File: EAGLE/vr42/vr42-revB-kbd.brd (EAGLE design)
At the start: 226.6 x 74.2 mm, 176 parts, among them M0 74HC589A_DT, M1 74HC589A_DT, M2 74HC589A_DT, M3 74HC589A_DT, M4 74HC589A_DT, M5 74HC589A_DT, U1 2N7002

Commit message: Rev 1.0B
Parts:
- removed C10, C11, C12, C13, C14, C15, C16, C17, C18, C19, C20, C21, C22, C23, C24, C25, C26, C27, C28, C7, C8, C9: 1uF, rcl:C0603
- added CA1, CA11, CA13, CA15, CA17, CA19, CA21, CA23, CA25, CA27, CA29, CA3, CA31, CA33, CA35, CA37, CA39, CA41, CA43, CA5, CA6, CA7, CA9: 1uF, rcl:C0603
- added LOGO1: OSHW-LOGOL, random_logos:OSHW-LOGO-L
- added U$3: TECSMITH-LOGOLONG, random_logos:TECSMITH-NAME
- added U$4: QMK_LOGO, random_logos:QMK_LOGO
- moved R45 12.4 mm to (210.8, 37.4), turned to 270 degrees
- moved R20 7.04 mm to (189.7, 68.5), turned to 180 degrees
- moved R36 7.00 mm to (108.7, 30.4), turned to 180 degrees
- moved R4 6.94 mm to (37.3, 68.5), turned to 180 degrees
- moved R11 6.90 mm to (94.4, 68.5), turned to 180 degrees
- moved R29 3.67 mm to (54.1, 24.9), turned to 270 degrees
- moved R27 3.39 mm to (32.6, 30.4), turned to 180 degrees
- moved R7 2.10 mm to (25.6, 45.0)
- moved C2 1.50 mm to (90.5, 57.0)
- moved C3 0.85 mm to (186.0, 57.6)
- moved R49 0.76 mm to (208.8, 37.4)
- moved C6 0.50 mm to (205.3, 20.1)
- renumbered I1 to A1, I10 to A10, I11 to A11, I12 to A12, I13 to A13, I14 to A14, I15 to A15, I16 to A16, I17 to A17, I18 to A18, I19 to A19, I2 to A2, I20 to A20, I21 to A21, I22 to A22, I23 to A23, I24 to A24, I25 to A25, I26 to A26, I27 to A27, I28 to A28, I29 to A29, I3 to A3, I30 to A30, I31 to A31, I32 to A32, I33 to A33, I34 to A34, I35 to A35, I36 to A36, I37 to A37, I38 to A38, I39 to A39, I4 to A4, I40 to A40, I41 to A41, I42 to A42, I43 to A43, I5 to A5, I6 to A6, I7 to A7, I8 to A8, I9 to A9
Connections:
- net GND: now also CA1.2, CA11.2, CA13.2, CA15.2, CA17.2, CA19.2, CA21.2, CA23.2, CA25.2, CA27.2, CA29.2, CA3.2, CA31.2, CA33.2, CA35.2, CA37.2, CA39.2, CA41.2, CA43.2, CA5.2, CA6.2, CA7.2, CA9.2; no longer C10.2, C11.2, C12.2, C13.2, C14.2, C15.2, C16.2, C17.2, C18.2, C19.2, C20.2, C21.2, C22.2, C23.2, C24.2, C25.2, C26.2, C27.2, C28.2, C7.2, C8.2, C9.2
- net VCC_1: now also CA1.1, CA11.1, CA13.1, CA15.1, CA17.1, CA19.1, CA21.1, CA23.1, CA25.1, CA27.1, CA29.1, CA3.1, CA31.1, CA33.1, CA35.1, CA37.1, CA39.1, CA41.1, CA43.1, CA5.1, CA6.1, CA7.1, CA9.1; no longer C10.1, C11.1, C12.1, C13.1, C14.1, C15.1, C16.1, C17.1, C18.1, C19.1, C20.1, C21.1, C22.1, C23.1, C24.1, C25.1, C26.1, C27.1, C28.1, C7.1, C8.1, C9.1
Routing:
- net VCC_1: track 0.00 -> 1149.0 mm, vias 0 -> 50
- net LATCH_MTX: track 266.4 -> 430.3 mm, vias 6 -> 7
- net SCK: track 252.8 -> 416.2 mm, vias 5 -> 8
- net CS_MTX: track 256.6 -> 418.0 mm, vias 3 -> 6
- net MATRIX_1_2: track 0.00 -> 109.9 mm, vias 0 -> 4
- net K50: track 5.67 -> 99.2 mm, vias 0 -> 6
- net VCC_2: track 1159.9 -> 1232.3 mm, vias 3 -> 12
- net MATRIX_0_1: track 0.00 -> 65.0 mm, vias 0 -> 2
- net K54: track 5.67 -> 70.0 mm, vias 0 -> 2
- net K44: track 5.67 -> 67.5 mm, vias 0 -> 2
- net K13: track 5.67 -> 66.4 mm, vias 0 -> 2
- net K17: track 5.67 -> 59.3 mm
- net K51: track 5.67 -> 59.2 mm, vias 0 -> 4
- net K40: track 5.67 -> 55.6 mm
- net K32: track 5.67 -> 48.9 mm
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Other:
- board text added: "(c) 2024 Vino Rodrigues https://c1k.it/vr42"
- board text added: "Revision: 1.0B"
- board text added: "VR42 Keyboard Key PCB"

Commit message: .
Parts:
- added U$5, U$6, U$7: FIDUCIAL, __temp_to_delete:FIDUCIAL
- moved I44 0.20 mm to (224.5, 51.3)
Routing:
- net VCC_1: track 1149.0 -> 1142.3 mm
- net VCC_2: track 1232.3 -> 1228.9 mm
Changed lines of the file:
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@@
 <element name="SW_Y" library="ts_keyboards" package="MX-5-PIN-HOTSWAP-PAD" value="MX-5-PIN-HOTSWAP-PAD" x="123.825" y="66.675" smashed="yes"/>
 <element name="SW_Z" library="ts_keyboards" package="MX-5-PIN-HOTSWAP-PAD" value="MX-5-PIN-HOTSWAP-PAD" x="42.8625" y="28.575" smashed="yes"/>
-<element name="I44" library="__temp_to_delete" package="ARGB" value="ARGB" x="224.3" y="51.3" smashed="yes" rot="R270"/>
+<element name="I44" library="__temp_to_delete" package="ARGB" value="ARGB" x="224.5" y="51.3" smashed="yes" rot="R270"/>
 <element name="M5" library="__untitled" package="TSSOP16" value="74HC589A_DT" x="209.5" y="23.5" smashed="yes" rot="MR270">
 <attribute name="NAME" x="209.9" y="24.4" size="1.016" layer="28" ratio="6" rot="SMR270"/>
@@
 <element name="U$4" library="random_logos" package="QMK_LOGO" value="QMK_LOGO" x="64" y="37" smashed="yes" rot="MR0"/>
 <element name="LOGO1" library="random_logos" package="OSHW-LOGO-L" value="OSHW-LOGOL" x="189" y="36" smashed="yes" rot="MR0"/>
+<element name="U$5" library="__temp_to_delete" package="FIDUCIAL" value="FIDUCIAL" x="3.5" y="72.5" smashed="yes"/>
+<element name="U$6" library="__temp_to_delete" package="FIDUCIAL" value="FIDUCIAL" x="224.5" y="20.5" smashed="yes"/>
+<element name="U$7" library="__temp_to_delete" package="FIDUCIAL" value="FIDUCIAL" x="72" y="3.5" smashed="yes"/>
 </elements>
 <signals>
@@
 <wire x1="205" y1="33.655" x2="221.615" y2="33.655" width="0.4064" layer="1"/>
 <wire x1="226.357" y1="70.1" x2="226.357" y2="52.705" width="0.4064" layer="1"/>
-<wire x1="226.357" y1="52.705" x2="226.357" y2="40.35" width="0.4064" layer="1"/>
 <wire x1="140.6525" y1="33.655" x2="121.6025" y2="33.655" width="0.4064" layer="1"/>
 <wire x1="121.6025" y1="33.655" x2="102.5525" y2="33.655" width="0.4064" layer="1"/>
@@
 <wire x1="40.65" y1="54.905" x2="38.0775" y2="54.905" width="0.4064" layer="1"/>
 <wire x1="38.0775" y1="54.905" x2="35.8775" y2="52.705" width="0.4064" layer="1"/>
-<wire x1="12.065" y1="71.755" x2="3.755" y2="71.755" width="0.4064" layer="1"/>
-<wire x1="3.755" y1="71.755" x2="2.243" y2="70.243" width="0.4064" layer="1"/>
-<wire x1="2.243" y1="70.243" x2="2.243" y2="56" width="0.4064" layer="1"/>
-<wire x1="2.243" y1="56" x2="2.243" y2="52.705" width="0.4064" layer="1"/>
 <wire x1="2.238" y1="52.705" x2="2.238" y2="33.655" width="0.4064" layer="1"/>
 <wire x1="14.44625" y1="14.605" x2="14.44625" y2="17.00375" width="0.4064" layer="1"/>
@@
 <wire x1="19.20875" y1="33.655" x2="2.238" y2="33.655" width="0.4064" layer="1"/>
 <wire x1="224.617" y1="17.617" x2="224.617" y2="14.605" width="0.4064" layer="16"/>
-<wire x1="225" y1="39" x2="225.007" y2="39" width="0.254" layer="1"/>
-<wire x1="226.357" y1="40.35" x2="225.007" y2="39" width="0.4064" layer="1"/>
-<via x="225" y="39" extent="1-16" drill="0.35"/>
-<wire x1="224.6" y1="38.6" x2="224.6" y2="33.672" width="0.4064" layer="16"/>
+<via x="225" y="37" extent="1-16" drill="0.35"/>
+<wire x1="224.6" y1="36.6" x2="224.6" y2="33.672" width="0.4064" layer="16"/>
 <wire x1="224.617" y1="33.655" x2="224.6" y2="33.672" width="0.254" layer="16"/>
-<wire x1="225" y1="39" x2="224.6" y2="38.6" width="0.4064" layer="16"/>
+<wire x1="225" y1="37" x2="224.6" y2="36.6" width="0.4064" layer="16"/>
 <wire x1="226.373" y1="30.099" x2="224.617" y2="31.855" width="0.4064" layer="16"/>
 <wire x1="224.617" y1="33.655" x2="224.617" y2="31.855" width="0.4064" layer="16"/>
@@
 <wire x1="14.44625" y1="52.705" x2="11.295" y2="52.705" width="0.4064" layer="1"/>
 <wire x1="11.295" y1="52.705" x2="8" y2="56" width="0.4064" layer="1"/>
-<wire x1="8" y1="56" x2="2.243" y2="56" width="0.4064" layer="1"/>
+<wire x1="8" y1="56" x2="4" y2="56" width="0.4064" layer="1"/>
 <wire x1="40.65" y1="54.905" x2="41.1028" y2="55.3578" width="0.4064" layer="1"/>
 <wire x1="41.1028" y1="55.3578" x2="52.2747" y2="55.3578" width="0.4064" layer="1"/>
@@
 <wire x1="203" y1="38" x2="205" y2="36" width="0.254" layer="1"/>
 <wire x1="205" y1="36" x2="205" y2="33.655" width="0.254" layer="1"/>
+<wire x1="4" y1="56" x2="3.8354" y2="55.8354" width="0.4064" layer="1"/>
+<wire x1="3.8354" y1="55.8354" x2="3.6539625" y2="55.8354" width="0.4064" layer="1"/>
+<wire x1="3.6539625" y1="55.8354" x2="2.243" y2="54.4244375" width="0.4064" layer="1"/>
+<wire x1="2.243" y1="54.4244375" x2="2.243" y2="52.705" width="0.4064" layer="1"/>
+<wire x1="12.065" y1="71.755" x2="13.82" y2="70" width="0.4064" layer="1"/>
+<wire x1="14.44625" y1="62.44625" x2="14.44625" y2="52.705" width="0.4064" layer="1"/>
+<wire x1="13.82" y1="70" x2="14.3" y2="70" width="0.4064" layer="1"/>
+<wire x1="14.3" y1="70" x2="16.7" y2="67.6" width="0.4064" layer="1"/>
+<wire x1="16.7" y1="67.6" x2="16.7" y2="64.7" width="0.4064" layer="1"/>
+<wire x1="16.7" y1="64.7" x2="14.44625" y2="62.44625" width="0.4064" layer="1"/>
+<wire x1="226.357" y1="38.357" x2="225" y2="37" width="0.4064" layer="1"/>
+<wire x1="226.357" y1="52.705" x2="226.357" y2="38.357" width="0.4064" layer="1"/>
 </signal>
 <signal name="K00">
@@
 <wire x1="85.40625" y1="3.724" x2="80.576" y2="3.724" width="0.254" layer="16"/>
 <wire x1="80.576" y1="3.724" x2="78.3" y2="6" width="0.254" layer="16"/>
-<wire x1="78.3" y1="6" x2="73.45" y2="6" width="0.254" layer="16"/>
-<wire x1="72.674" y1="5.224" x2="58" y2="5.224" width="0.254" layer="16"/>
-<wire x1="58" y1="5.224" x2="57.81175" y2="5.224" width="0.254" layer="16"/>
-<wire x1="73.45" y1="6" x2="72.674" y2="5.224" width="0.254" layer="16"/>
-<wire x1="57.46875" y1="5.224" x2="57.81175" y2="5.224" width="0.254" layer="16"/>
+<wire x1="78.3" y1="6" x2="69.45" y2="6" width="0.254" layer="16"/>
+<wire x1="68.674" y1="5.224" x2="57.46875" y2="5.224" width="0.254" layer="16"/>
+<wire x1="69.45" y1="6" x2="68.674" y2="5.224" width="0.254" layer="16"/>
 </signal>
 <signal name="N$33">
@@
 <wire x1="210.080775" y1="59.2192" x2="216.15759375" y2="59.2192" width="0.4064" layer="16"/>
 <wire x1="216.66999375" y1="58.7068" x2="223.7068" y2="58.7068" width="0.4064" layer="16"/>
-<wire x1="224.3" y1="51.3" x2="224.3" y2="58.1136" width="0.4064" layer="16"/>
 <wire x1="224.3" y1="58.1136" x2="223.7068" y2="58.7068" width="0.4064" layer="16"/>
-<wire x1="219" y1="46" x2="219" y2="43" width="0.4064" layer="16"/>
-<wire x1="219" y1="43" x2="215.6548" y2="39.6548" width="0.4064" layer="16"/>
 <wire x1="206.8548" y1="39.6548" x2="206.85" y2="39.65" width="0.4064" layer="16"/>
 <via x="206.85" y="39.65" extent="1-16" drill="0.35"/>
@@
 <wire x1="66.65" y1="39.6548" x2="47.85" y2="39.6548" width="0.4064" layer="1"/>
 <wire x1="47.85" y1="39.6548" x2="28.5" y2="39.6548" width="0.4064" layer="1"/>
-<wire x1="224.3" y1="51.3" x2="219" y2="46" width="0.4064" layer="16"/>
-<wire x1="215.6548" y1="39.6548" x2="206.8548" y2="39.6548" width="0.4064" layer="16"/>
+<wire x1="206.8548" y1="39.6548" x2="215.6548" y2="39.6548" width="0.4064" layer="16"/>
 <wire x1="206.8452" y1="39.6548" x2="179.45" y2="39.6548" width="0.4064" layer="1"/>
 <wire x1="179.45" y1="39.6548" x2="168" y2="39.6548" width="0.4064" layer="1"/>
@@
 <wire x1="192.7" y1="16.55" x2="192.3842" y2="16.2342" width="0.4064" layer="1"/>
 <wire x1="192.3842" y1="16.2342" x2="191.45909375" y2="16.2342" width="0.4064" layer="1"/>
+<wire x1="221" y1="47.8" x2="224.5" y2="51.3" width="0.4064" layer="16"/>
+<wire x1="215.6548" y1="39.6548" x2="221" y2="45" width="0.4064" layer="16"/>
+<wire x1="221" y1="45" x2="221" y2="47.8" width="0.4064" layer="16"/>
 </signal>
 <signal name="N$1">
@@
 <contactref element="I44" pad="D"/>
 <wire x1="221.775" y1="62.376" x2="225.324" y2="62.376" width="0.254" layer="16"/>
-<wire x1="226.457" y1="50.917" x2="224.3" y2="48.76" width="0.254" layer="16"/>
 <wire x1="225.324" y1="62.376" x2="226.457" y2="61.243" width="0.254" layer="16"/>
-<wire x1="226.457" y1="61.243" x2="226.457" y2="50.917" width="0.254" layer="16"/>
+<wire x1="226.457" y1="61.243" x2="226.457" y2="51" width="0.254" layer="16"/>
+<wire x1="226.457" y1="51" x2="226.457" y2="50.917" width="0.254" layer="16"/>
+<wire x1="226.457" y1="50.917" x2="226.457" y2="50.717" width="0.254" layer="16"/>
+<wire x1="226.457" y1="50.717" x2="224.5" y2="48.76" width="0.254" layer="16"/>
 </signal>
 <signal name="MATRIX_2_3">

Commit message: .
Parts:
- added U$8: TECSMITH-LOGOLONG, random_logos:TECSMITH-NAME

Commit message: .
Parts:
- flipped I44 to the bottom
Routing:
- net VCC_1: track 1142.3 -> 1149.2 mm, vias 50 -> 60
- net VCC_2: track 1228.9 -> 1231.8 mm, vias 12 -> 16
- net K43: track 36.4 -> 35.7 mm
- net K23: track 43.8 -> 44.4 mm
- net N$40: track 17.1 -> 17.7 mm
- net K27: track 27.3 -> 27.9 mm
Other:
- outline, holes or cut-outs redrawn
- board text added: "1.25U"
- board text added: "1.75U"
- board text added: "2.25U"
- board text added: "2.75U"
- board text added: "2024 Vino Rodrigues"
- board text added: "5V"
- board text added: "A"
- board text added: "ARGB"
- board text added: "B"
- board text added: "Bsp"
- board text added: "C"
- board text added: "Ctl"
- board text added: "D"
- board text added: "Data"
- board text added: "Del"
- board text added: "E"
- board text added: "Ent"
- board text added: "Esc"
- board text added: "F"
- board text added: "G"
- board text added: "Gnd"
- board text added: "H"
- board text added: "I"
- board text added: "J"
- board text added: "K"
- board text added: "L"
- board text added: "M"
- board text added: "N"
- board text added: "O"
- board text added: "P"
- board text added: "Q"
- board text added: "R"
- board text added: "S"
- board text added: "Sft"
- board text added: "T"
- board text added: "Tab"
- board text added: "U"
- board text added: "V"
- board text added: "VR42"
- board text added: "W"
- board text added: "X"
- board text added: "Y"
- board text added: "Z"

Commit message: Beta 1
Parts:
- added A1.5: SK6812-E-REVERSE_V2, tecsmith_keyboards:SK6812-E-MILL_V2
- A1, A10, A11, A12, A13, A14, A15, A16, A17, A18, A19, A2, A20, A21, A22, A23, A24, A25, A26, A27, A28, A29, A3, A30, A31, A32, A33, A34, A35, A36, A37, A38, A39, A4, A40, A41, A42, A43, A5, A6, A7, A8, A9: value SK6812-E-REVERSE -> SK6812-E-REVERSE_V2; device ts_keyboards:SK6812-E-MILL -> tecsmith_keyboards:SK6812-E-MILL_V2
- moved CA1 4.13 mm to (166.8, 9.48)
- moved LOGO1 3.24 mm to (191.7, 37.8)
- moved A1 3.17 mm to (166.7, 12.7), turned to 180 degrees
- moved U$4 2.15 mm to (66.1, 36.9)
- moved CA3 0.62 mm to (194.4, 6.05)
- moved CA43 0.35 mm to (224.3, 60.9)
- moved U$5 0.07 mm to (3.45, 72.5)
- renumbered KB_MTX to KB_MATRIX
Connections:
- removed net N$46: A1.2-DOUT, A2.4-DIN
- new net N$10: A1.2-DOUT, A1.5.4-DIN
- new net N$9: A1.5.2-DOUT, A2.4-DIN
- net GND: now also A1.5.3-GND
- net VCC_1: now also A1.5.1-VDD
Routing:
- net N$9: track 0.00 -> 85.9 mm, vias 0 -> 2
- net N$46: track 84.4 -> 0.00 mm, vias 2 -> 0
- net VCC_1: track 1149.2 -> 1173.4 mm
- net GND: track 2.91 -> 18.6 mm, vias 174 -> 207
- net N$10: track 0.00 -> 10.4 mm
- net N$1: track 19.6 -> 9.58 mm
- net VCC_2: track 1231.8 -> 1234.0 mm, vias 16 -> 17
- net K50: track 99.2 -> 100.8 mm
- net N$40: track 17.7 -> 18.8 mm
- net N$52: track 41.1 -> 42.0 mm
- net N$41: track 17.7 -> 17.1 mm
- net K23: track 44.4 -> 44.9 mm, vias 2 -> 4
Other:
- board text added: "VR42 Keyboard Switch PCB"
- board text removed: "VR42 Keyboard Key PCB"

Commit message: .
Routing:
- net VCC_2: track 1234.0 -> 1236.0 mm
- net K41: track 43.1 -> 44.0 mm
- net N$50: track 14.7 -> 15.4 mm
- net N$34: track 17.1 -> 17.8 mm
- net VCC_1: track 1173.4 -> 1172.7 mm
- net GND: vias 207 -> 208

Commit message: .
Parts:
- moved U$1 10.1 mm to (171.4, 60.2)
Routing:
- net K27: track 27.9 -> 32.2 mm
- net K23: track 44.9 -> 49.2 mm
- net GND: track 18.6 -> 21.3 mm, vias 208 -> 212
- net K26: track 28.2 -> 30.8 mm
- net K04: track 48.5 -> 50.5 mm
- net K01: track 32.0 -> 33.5 mm
- net K05: track 30.8 -> 31.8 mm
- net VCC_1: track 1172.7 -> 1173.4 mm, vias 60 -> 59
- net K25: track 41.4 -> 40.7 mm
- net K00: track 50.6 -> 51.3 mm

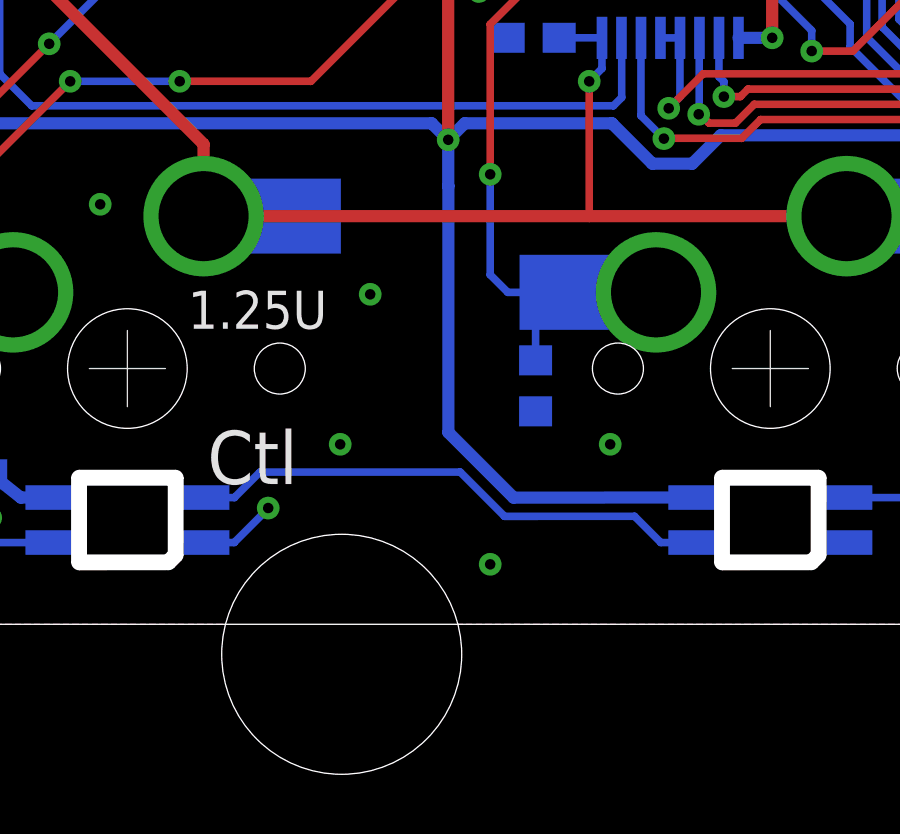
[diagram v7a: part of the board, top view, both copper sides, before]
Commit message: fixed signal pairs
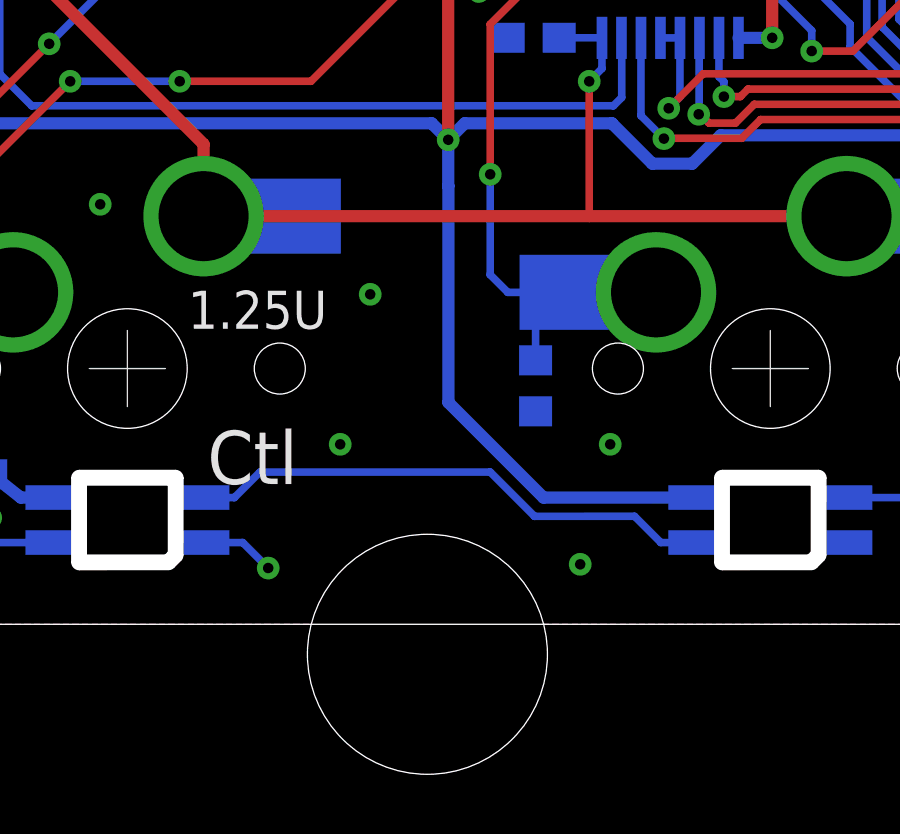
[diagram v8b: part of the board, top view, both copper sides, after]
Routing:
- net VCC_1: track 1173.4 -> 1172.8 mm
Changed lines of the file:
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@@
 <text x="13.925" y="48.95" size="1.27" layer="25">1.25U</text>
 <hole x="19.05" y="76.2" drill="8"/>
-<hole x="19.05" y="0" drill="8"/>
+<hole x="21.9075" y="0" drill="8"/>
 <hole x="95.25" y="76.2" drill="8"/>
 <hole x="114.3" y="0" drill="8"/>
@@
 <via x="20" y="12" extent="1-16" drill="0.35"/>
 <via x="28" y="7" extent="1-16" drill="0.35"/>
-<via x="24" y="3" extent="1-16" drill="0.35"/>
+<via x="27" y="3" extent="1-16" drill="0.35"/>
 <via x="3.7" y="16.1" extent="1-16" drill="0.35"/>
 <via x="11" y="15" extent="1-16" drill="0.35"/>
@@
 <via x="225.64725" y="69.484875" extent="1-16" drill="0.35"/>
 <via x="223.8613125" y="73.7473125" extent="1-16" drill="0.35"/>
-<via x="16.6" y="4.875" extent="1-16" drill="0.35"/>
+<via x="16.6" y="2.875" extent="1-16" drill="0.35"/>
 <via x="196.357875" y="53.61384375" extent="1-16" drill="0.35"/>
 <via x="193.51228125" y="57.3166875" extent="1-16" drill="0.35"/>
 <via x="192.65503125" y="55.20928125" extent="1-16" drill="0.35"/>
 <via x="25.41984375" y="59.6265" extent="1-16" drill="0.35"/>
-<wire x1="16.6" y1="4.875" x2="16.6" y2="4.85909375" width="0.254" layer="16"/>
-<wire x1="14.40625" y1="3.725" x2="15.46590625" y2="3.725" width="0.254" layer="16"/>
-<wire x1="16.6" y1="4.85909375" x2="15.46590625" y2="3.725" width="0.254" layer="16"/>
+<wire x1="16.6" y1="2.875" x2="15.75" y2="3.725" width="0.254" layer="16"/>
+<wire x1="15.75" y1="3.725" x2="14.40625" y2="3.725" width="0.254" layer="16"/>
 </signal>
 <signal name="VCC_2">
@@
 <wire x1="30.8375" y1="3.725" x2="29.6875" y2="3.725" width="0.254" layer="16"/>
 <wire x1="29.6875" y1="3.725" x2="28.812746875" y2="4.599753125" width="0.254" layer="16"/>
-<wire x1="28.812746875" y1="4.599753125" x2="24.47581875" y2="4.59918125" width="0.254" layer="16"/>
-<wire x1="23.001" y1="6.074" x2="16.32425" y2="6.074" width="0.254" layer="16"/>
+<wire x1="28.812746875" y1="4.599753125" x2="25.4756875" y2="4.5993125" width="0.254" layer="16"/>
+<wire x1="24.001" y1="6.074" x2="16.32425" y2="6.074" width="0.254" layer="16"/>
 <wire x1="16.32425" y1="6.074" x2="15.473284375" y2="5.223034375" width="0.254" layer="16"/>
-<wire x1="24.47581875" y1="4.59918125" x2="23.001" y2="6.074" width="0.254" layer="16"/>
+<wire x1="25.4756875" y1="4.5993125" x2="24.001" y2="6.074" width="0.254" layer="16"/>
 <wire x1="14.40625" y1="5.225" x2="15.473284375" y2="5.223034375" width="0.254" layer="16"/>
 </signal>
@@
 <wire x1="2.2192" y1="16.3192" x2="3.6" y2="17.7" width="0.4064" layer="1"/>
 <via x="3.6" y="17.7" extent="1-16" drill="0.35"/>
-<wire x1="30.8375" y1="5.225" x2="24.776" y2="5.224" width="0.4064" layer="16"/>
-<wire x1="22.6068" y1="7.3932" x2="22.6068" y2="15.6068" width="0.4064" layer="16"/>
-<wire x1="24.776" y1="5.224" x2="22.6068" y2="7.3932" width="0.4064" layer="16"/>
+<wire x1="30.8375" y1="5.225" x2="25.775834375" y2="5.224165625" width="0.4064" layer="16"/>
+<wire x1="22.6068" y1="8.3932" x2="22.6068" y2="15.6068" width="0.4064" layer="16"/>
+<wire x1="25.775834375" y1="5.224165625" x2="22.6068" y2="8.3932" width="0.4064" layer="16"/>
 <via x="130.85" y="4.65" extent="1-16" drill="0.35"/>
 <wire x1="130.85" y1="4.65" x2="128.45" y2="4.65" width="0.4064" layer="1"/>
